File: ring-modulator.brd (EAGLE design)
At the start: 25.4 x 26.3 mm, 29 parts, among them IC1 TL072D, U1 MC1496DR2G

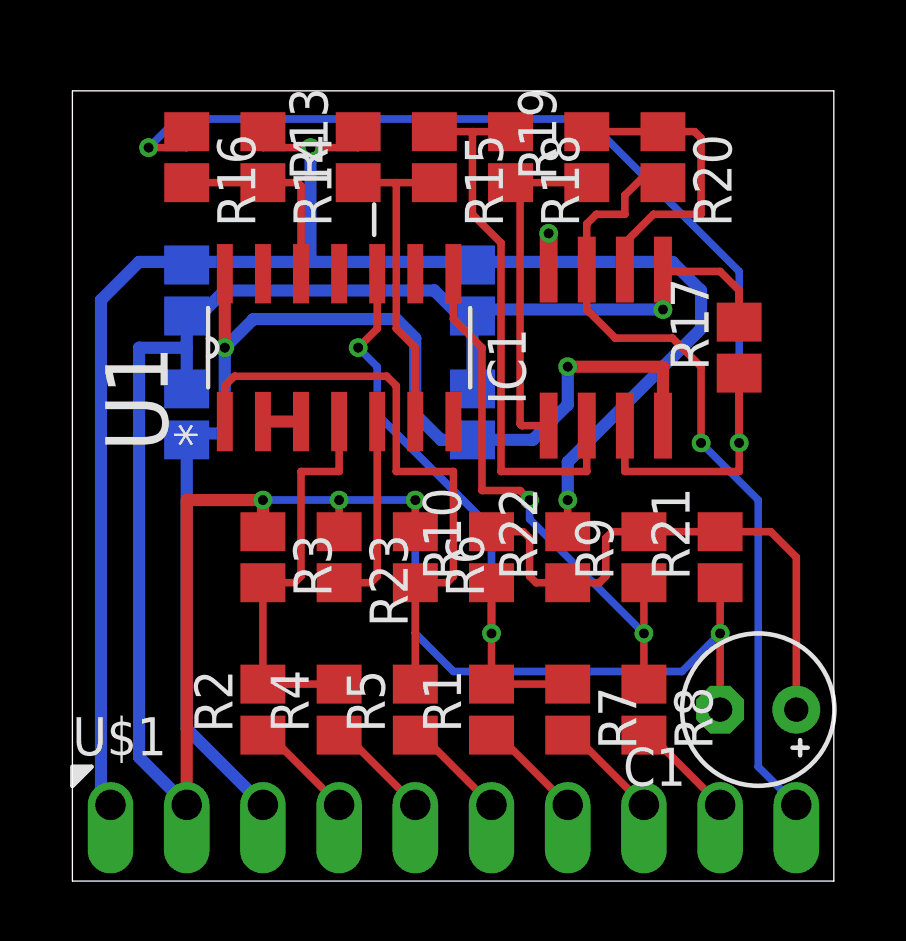
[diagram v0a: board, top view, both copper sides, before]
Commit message: Part and connector names
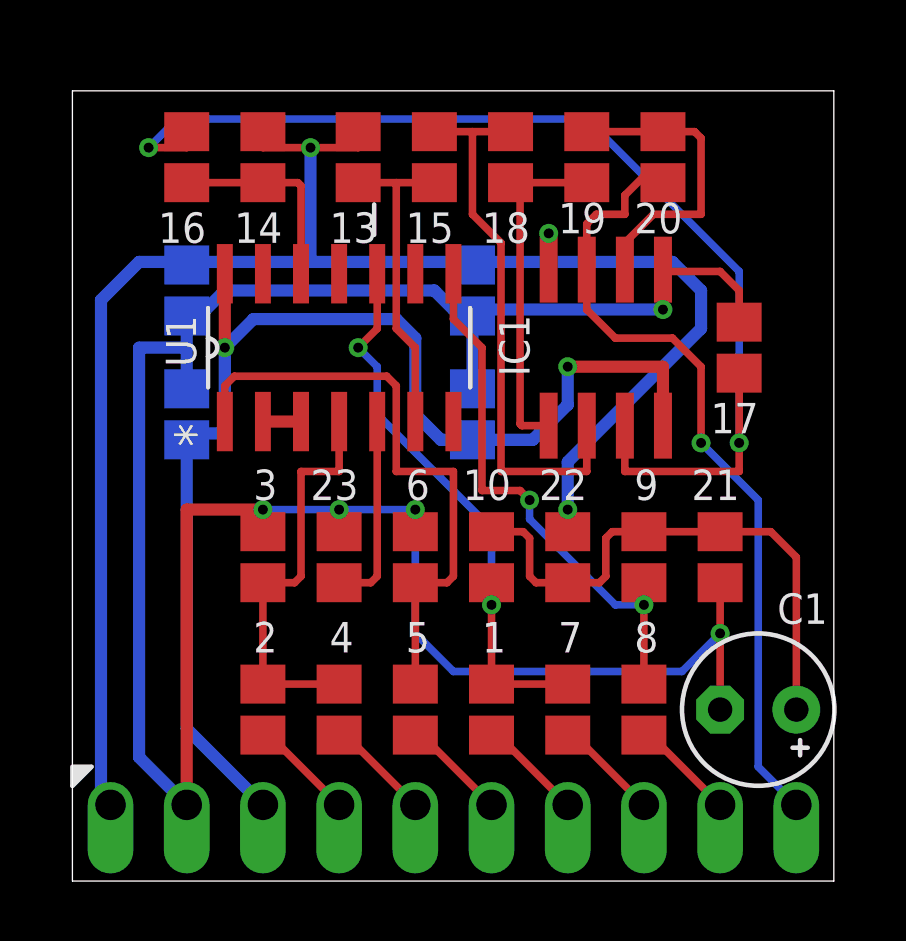
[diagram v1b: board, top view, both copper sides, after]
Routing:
- net GND: track 85.9 -> 84.3 mm
- net N$2: track 20.0 -> 19.1 mm
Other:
- board text added: "+15v"
- board text added: "-15v"
- board text added: "1"
- board text added: "10"
- board text added: "13"
- board text added: "14"
- board text added: "15"
- board text added: "16"
- board text added: "17"
- board text added: "18"
- board text added: "19"
- board text added: "2"
- board text added: "20"
- board text added: "21"
- board text added: "22"
- board text added: "23"
- board text added: "3"
- board text added: "4"
- board text added: "5"
- board text added: "6"
- board text added: "7"
- board text added: "8"
- board text added: "9"
- board text added: "C1"
- board text added: "Carrier"
- board text added: "Gnd"
- board text added: "IC1"
- board text added: "Out"
- board text added: "Signal"
- board text added: "Trim"
- board text added: "U1"

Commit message: Added logo
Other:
- board size 25.4 x 26.3 mm -> 25.4 x 26.4 mm
- board text added: "4B&V"
- board text added: "XRINGMOD"
- board text added: "v1.0"
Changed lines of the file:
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@@
 <layer number="23" name="tOrigins" color="15" fill="1" visible="yes" active="yes"/>
 <layer number="24" name="bOrigins" color="15" fill="1" visible="yes" active="yes"/>
-<layer number="25" name="tNames" color="7" fill="1" visible="no" active="yes"/>
-<layer number="26" name="bNames" color="7" fill="1" visible="yes" active="yes"/>
+<layer number="25" name="tNames" color="7" fill="1" visible="yes" active="yes"/>
+<layer number="26" name="bNames" color="7" fill="1" visible="no" active="yes"/>
 <layer number="27" name="tValues" color="7" fill="1" visible="no" active="yes"/>
 <layer number="28" name="bValues" color="7" fill="1" visible="no" active="yes"/>
@@
 <wire x1="0" y1="0" x2="25.38" y2="0" width="0" layer="20"/>
 <wire x1="25.38" y1="0" x2="25.38" y2="26.34" width="0" layer="20"/>
-<wire x1="25.38" y1="26.34" x2="0" y2="26.34" width="0" layer="20"/>
-<wire x1="0" y1="26.34" x2="0" y2="0" width="0" layer="20"/>
+<wire x1="25.38" y1="26.34" x2="2.8575" y2="26.3525" width="0" layer="20"/>
+<wire x1="0" y1="23.495" x2="0" y2="0" width="0" layer="20"/>
 <text x="6.0325" y="7.62" size="1.016" layer="25" font="vector">2</text>
 <text x="8.5725" y="7.62" size="1.016" layer="25" font="vector">4</text>
@@
 <text x="21.2725" y="14.9225" size="1.016" layer="25" font="vector">17</text>
 <text x="23.495" y="8.5725" size="1.016" layer="25" font="vector">C1</text>
-<text x="4.1275" y="17.145" size="1.016" layer="25" font="vector" rot="R90">U1</text>
-<text x="15.24" y="16.8275" size="1.016" layer="25" font="vector" rot="R90">IC1</text>
+<text x="8.5725" y="18.415" size="1.016" layer="25" font="vector" rot="R180">U1</text>
+<text x="19.05" y="18.415" size="1.016" layer="25" font="vector" rot="R180">IC1</text>
 <text x="0.635" y="3.81" size="1.27" layer="26" font="vector" rot="MR90">+15v</text>
 <text x="5.715" y="3.81" size="1.27" layer="26" font="vector" rot="MR90">-15v</text>
@@
 <wire x1="20.0025" y1="5.08" x2="20.0025" y2="4.445" width="0.1016" layer="26"/>
 <wire x1="20.0025" y1="4.445" x2="19.05" y2="4.445" width="0.1016" layer="26"/>
+<wire x1="0" y1="23.495" x2="2.8575" y2="26.3525" width="0" layer="20"/>
+<circle x="5.08" y="16.8275" radius="0.127" width="0.4064" layer="25"/>
+<circle x="15.875" y="16.8275" radius="0.127" width="0.4064" layer="25"/>
+<text x="2.8575" y="6.0325" size="2.1844" layer="25" font="vector" ratio="16" rot="R90">XRINGMOD</text>
+<text x="20.955" y="24.13" size="1.27" layer="25" font="vector">v1.0</text>
+<text x="24.765" y="14.9225" size="1.27" layer="25" font="vector" rot="R90">4B&amp;V</text>
 </plain>
 <attributes>
